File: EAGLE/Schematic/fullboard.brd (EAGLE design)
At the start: 90.8 x 77.1 mm, 91 parts, among them CN1 B4B-ZR, CN2 B4B-ZR, CN3 B4B-ZR, IC1 IFX007T, IC2 IFX007T, IC3 IFX007T, IC4 IFX007T, IC5 FT232RL-REEL, IC6 LDL1117S33R, IC7 AZ1117IH, J1 10118193-0001LF, Q1 8MHz ±10ppm Crystal 18pF 80 O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, Q2 AOD4189, SW1 TR1-SPST, U1 ATXMEGA128A3U-AU

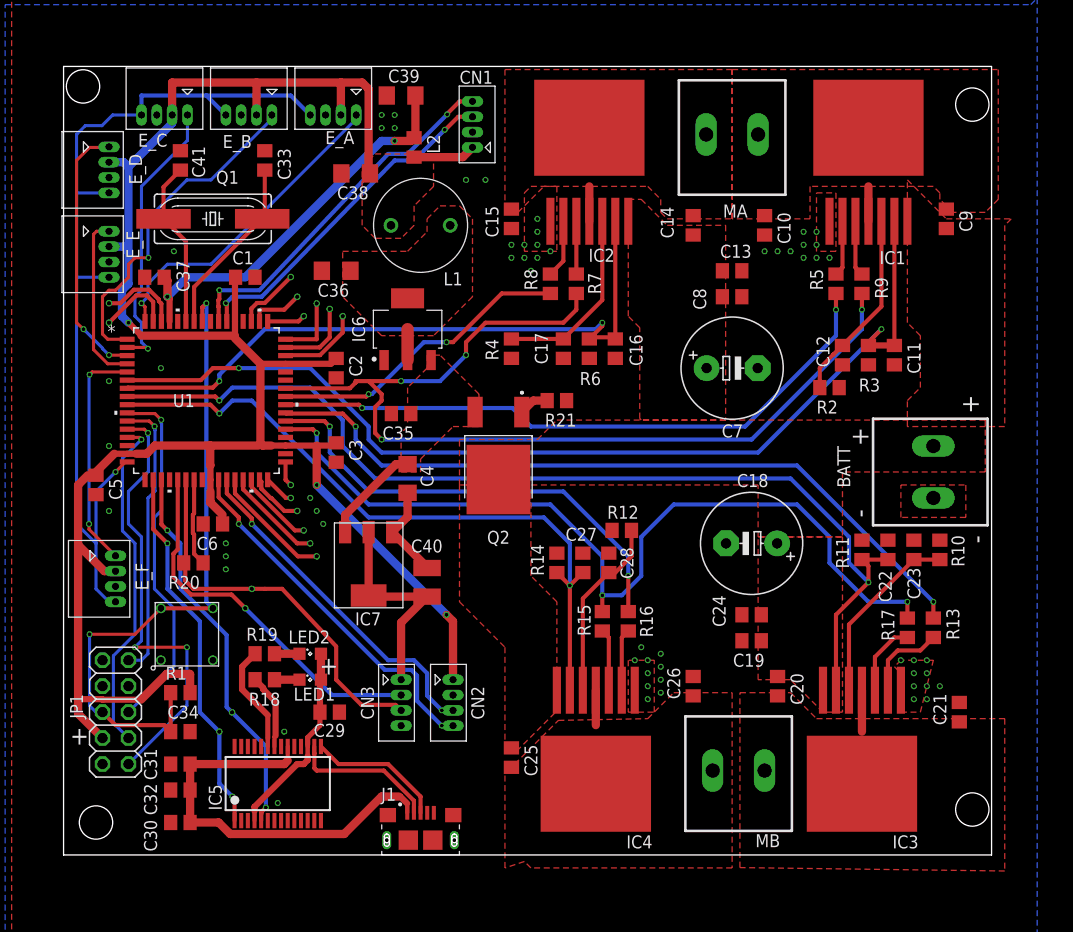
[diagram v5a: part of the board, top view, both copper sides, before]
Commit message: v0.6
Changes
* Adjusted part locations for increased fastener backup
* Added text label
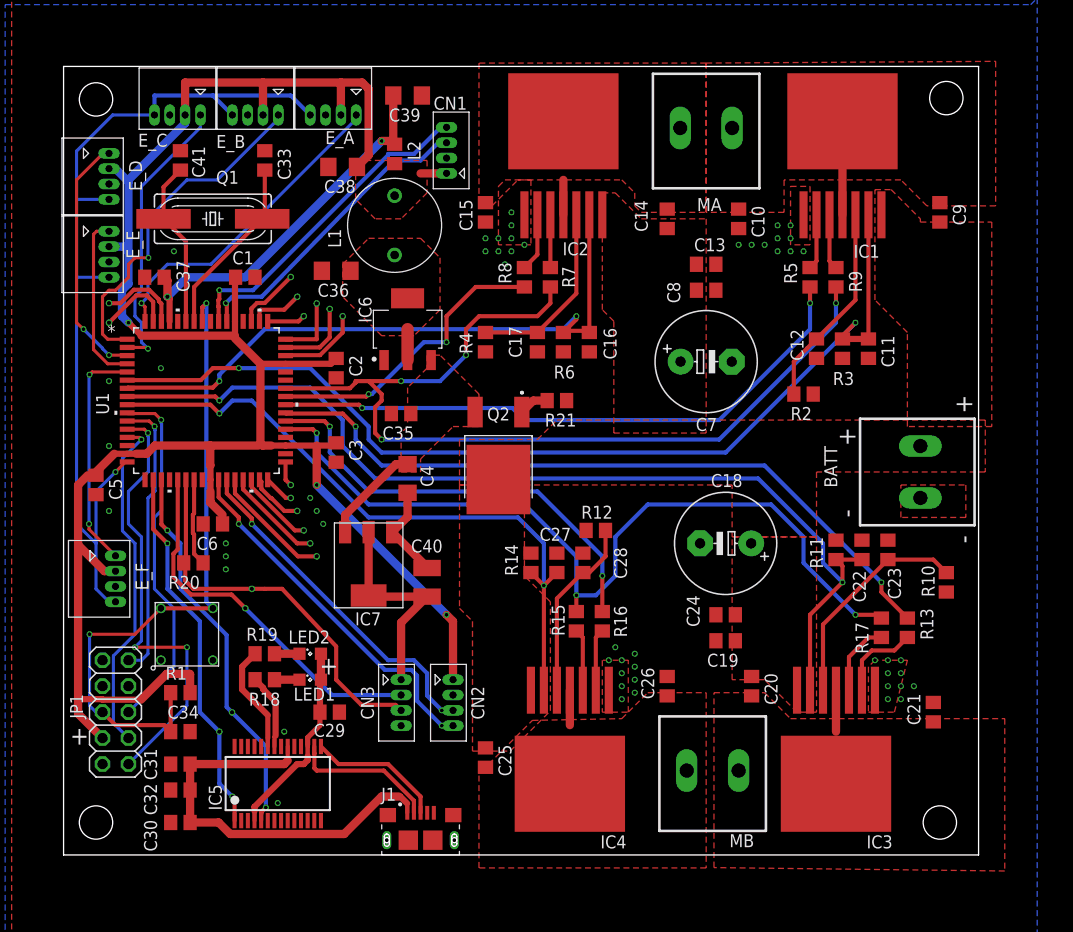
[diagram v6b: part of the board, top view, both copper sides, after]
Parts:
- moved CN1 3.59 mm to (37.5, 66.7)
- moved R10 3.24 mm to (86.4, 26.7), turned to 270 degrees
- moved C11 2.62 mm to (78.7, 49.5)
- moved C12 2.62 mm to (73.7, 49.5)
- moved C17 2.62 mm to (46.4, 50.2)
- moved R2 2.62 mm to (72.4, 45.1)
- moved R9 2.62 mm to (75.6, 56.5)
- moved C15 2.62 mm to (41.3, 62.9)
- moved IC2 2.62 mm to (48.9, 60.3)
- moved MA 2.62 mm to (62.9, 71.1)
- moved C13 2.62 mm to (62.9, 57.8)
- moved C14 2.62 mm to (59.1, 62.2)
- moved C16 2.62 mm to (51.4, 50.2)
- moved C7 2.62 mm to (62.9, 48.3)
- moved C8 2.62 mm to (62.9, 55.2)
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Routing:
- net +3V3: track 216.3 -> 212.1 mm
- net EN_A: track 95.8 -> 92.0 mm
- net EB_A: track 35.8 -> 32.0 mm, vias 2 -> 1
- net N$10: track 18.0 -> 21.7 mm
- net EA_A: track 33.6 -> 30.0 mm, vias 2 -> 1
- net EN_B: track 85.4 -> 82.0 mm
- net FWD_B: track 73.4 -> 70.5 mm
- net CSF_B: track 101.0 -> 98.1 mm
- net FWD_A: track 62.5 -> 59.7 mm
- net BCK_B: track 45.9 -> 43.4 mm
- net CSB_B: track 67.9 -> 65.4 mm
- net CSF_A: track 100.2 -> 98.0 mm
- net CSB_A: track 65.8 -> 63.5 mm
- net EDGE_D: track 26.0 -> 24.6 mm
- net MA_1: track 3.41 -> 4.69 mm
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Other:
- board size 90.8 x 77.1 mm -> 89.5 x 77.1 mm
- board text added: "California Polytechnic State University of San Luis Obispo ME 507 - Mechanical Control System Design Fall 2019 - SumoBot v1.0 Ryan Forsberg & Philippe Habets"

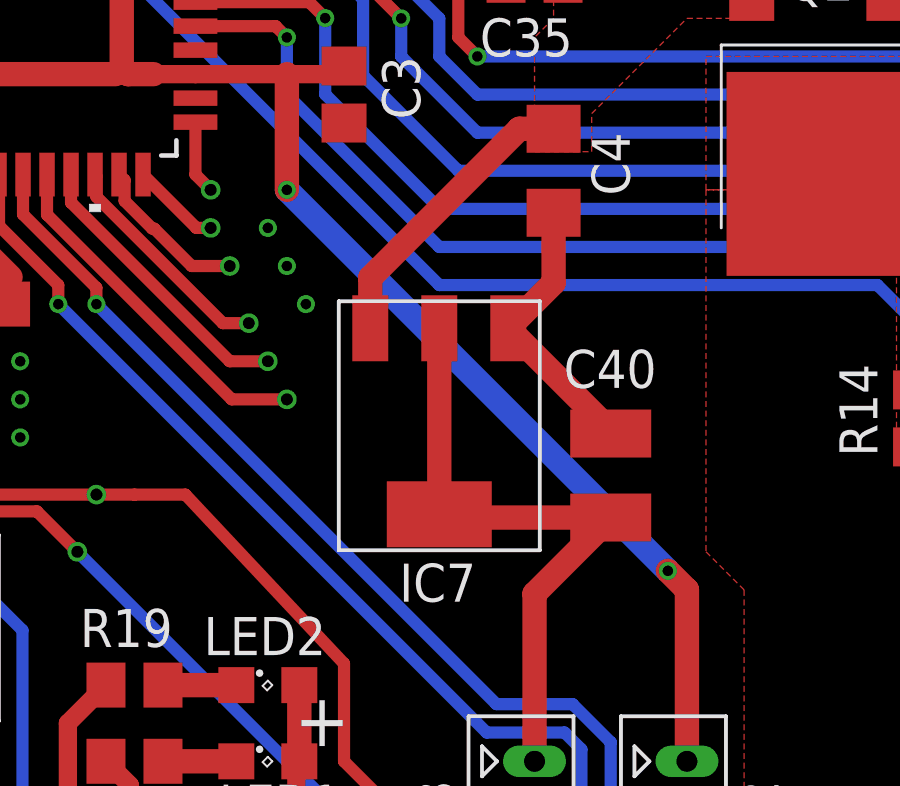
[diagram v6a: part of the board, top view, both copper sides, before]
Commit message: v0.7
Changes
* Create solderable vias for +3.3V and +5V
* Add labels for those vias
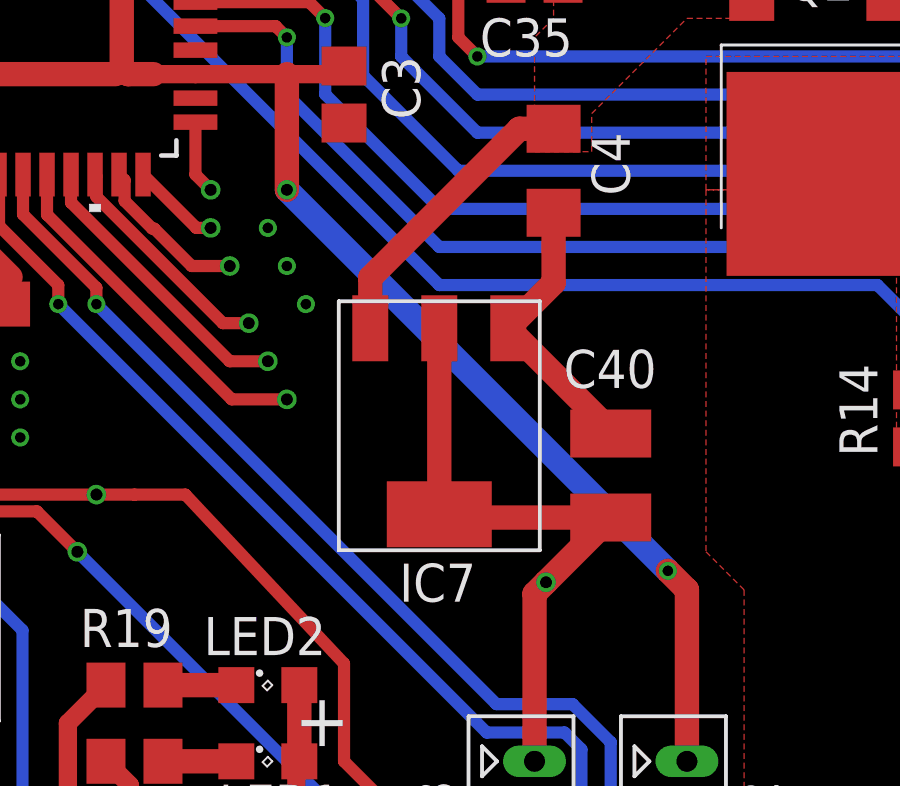
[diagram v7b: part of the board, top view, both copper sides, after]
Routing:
- net +5V: vias 0 -> 1
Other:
- board text added: "+3.3V"
- board text added: "+5V"
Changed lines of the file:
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@@
 <?xml version="1.0" encoding="utf-8"?>
 <!DOCTYPE eagle SYSTEM "eagle.dtd">
-<eagle version="9.4.2">
+<eagle version="9.5.1">
 <drawing>
 <settings>
@@
 <setting verticaltext="up"/>
 </settings>
-<grid distance="25" unitdist="mil" unit="mm" style="lines" multiple="1" display="no" altdistance="5" altunitdist="mil" altunit="mil"/>
+<grid distance="25" unitdist="mil" unit="mil" style="lines" multiple="1" display="no" altdistance="5" altunitdist="mil" altunit="mil"/>
 <layers>
 <layer number="1" name="Top" color="4" fill="1" visible="yes" active="yes"/>
@@
 Fall 2019 - SumoBot v1.0
 Ryan Forsberg &amp; Philippe Habets</text>
+<text x="35.56" y="21.59" size="1.016" layer="26" rot="MR0">+5V</text>
+<text x="29.21" y="35.56" size="1.016" layer="26" rot="MR0">+3.3V</text>
 </plain>
 <attributes>
@@
 <wire x1="38.1" y1="22.86" x2="38.1" y2="17.145" width="0.8128" layer="1"/>
 <wire x1="37.465" y1="23.495" x2="24.765" y2="36.195" width="0.8128" layer="16"/>
-<via x="24.765" y="36.195" extent="1-16" drill="0.35"/>
+<via x="24.765" y="36.195" extent="1-16" drill="0.4"/>
 <wire x1="24.765" y1="36.195" x2="24.765" y2="40.05" width="0.8128" layer="1"/>
 <wire x1="10.0972" y1="17.7172" x2="12.33538125" y2="17.7172" width="0.8128" layer="1"/>
@@
 <wire x1="29.845" y1="25.38" x2="29.845" y2="31.58" width="0.8128" layer="1"/>
 <wire x1="33.02" y1="17.145" x2="33.02" y2="22.73" width="0.8128" layer="1"/>
-<wire x1="33.02" y1="22.73" x2="35.56" y2="25.27" width="0.8128" layer="1"/>
+<wire x1="33.02" y1="22.73" x2="33.4025" y2="23.1125" width="0.8128" layer="1"/>
+<wire x1="35.56" y1="25.27" x2="33.4025" y2="23.1125" width="0.8128" layer="1"/>
+<via x="33.4025" y="23.1125" extent="1-16" drill="0.4"/>
 </signal>
 <signal name="N$20">

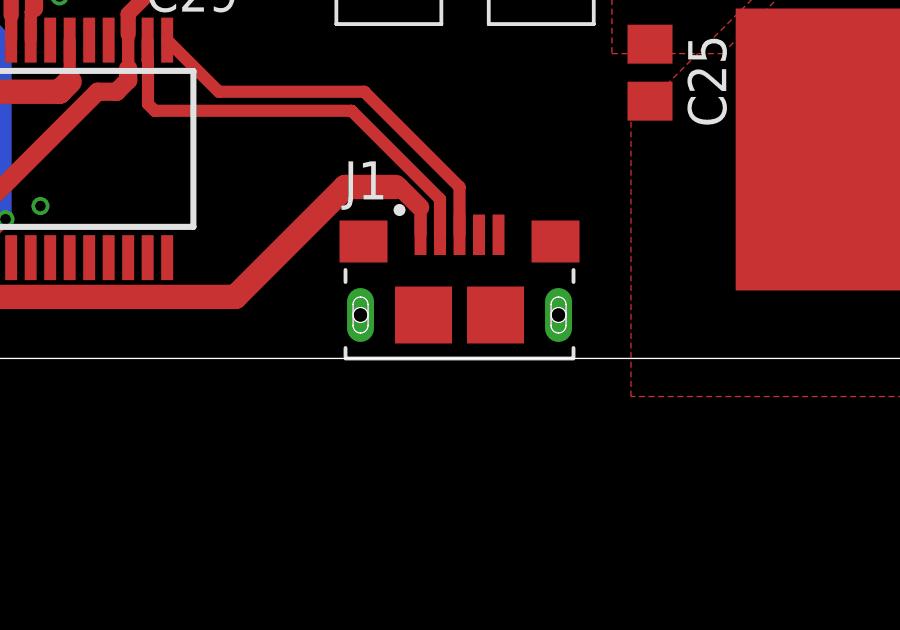
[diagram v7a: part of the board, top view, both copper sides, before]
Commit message: v0.8
Fixed the USB connector footprint
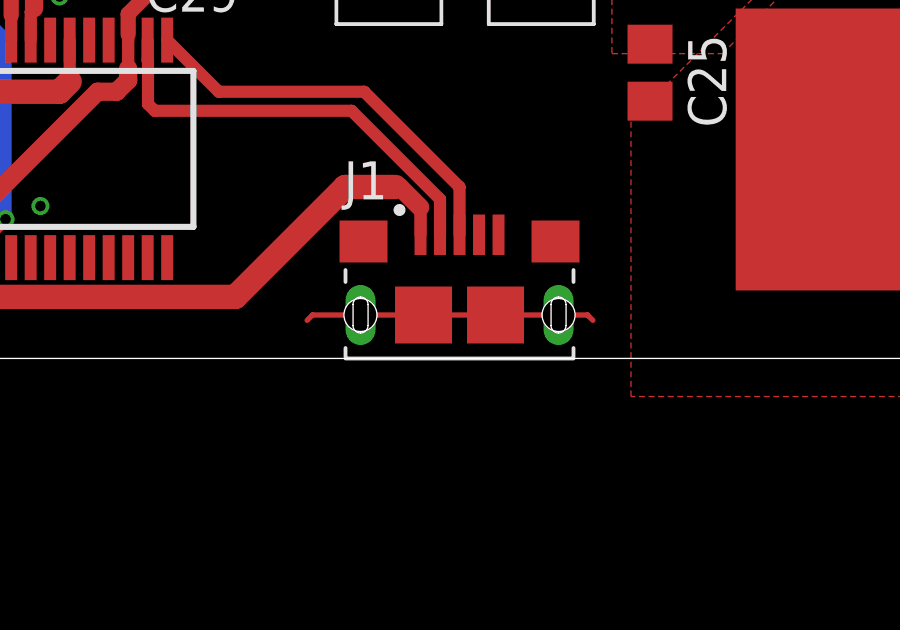
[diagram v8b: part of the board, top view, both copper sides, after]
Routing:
- net GND: track 0.00 -> 9.67 mm
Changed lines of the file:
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@@
 <drawing>
 <settings>
-<setting alwaysvectorfont="yes"/>
+<setting alwaysvectorfont="no"/>
 <setting verticaltext="up"/>
 </settings>
@@
 <vertex x="81.915" y="33.02"/>
 </polygon>
+<wire x1="30.0228" y1="1.4478" x2="29.845" y2="1.27" width="0.1778" layer="1"/>
+<wire x1="38.225" y1="1.4478" x2="39.1922" y2="1.4478" width="0.1778" layer="1"/>
+<wire x1="39.1922" y1="1.4478" x2="39.37" y2="1.27" width="0.1778" layer="1"/>
+<wire x1="38.225" y1="1.4478" x2="30.0228" y2="1.4478" width="0.1778" layer="1"/>
+<wire x1="29.845" y1="1.27" x2="31.625" y2="1.4478" width="0" layer="19" extent="1-1"/>
 </signal>
 <signal name="!RESET">
